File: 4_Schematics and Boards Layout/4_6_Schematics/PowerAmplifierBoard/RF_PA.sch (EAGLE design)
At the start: 25 parts, among them J1 142-0731-211, J2 142-0731-211, X2 22-23-2021, X3 22-23-2031

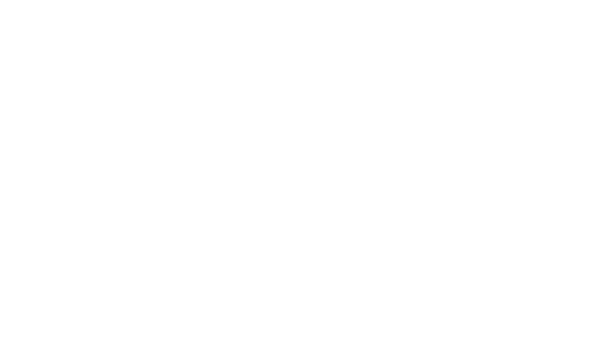
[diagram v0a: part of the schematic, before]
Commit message: feat(hw): gate-bias fail-safe, negative-rail margin, PA drain bulk (Lane B B2.2/B1.5/B2.3)
B2.2 -- and this is the finding that matters.  Every one of the 16 gate-bias
channels is an inverting amplifier referenced to ground (Vout = -(Rf/Rin) x VDAC,
+ input on GND), so a DAC in reset puts **0 V on all 16 gates**.  QPA2962 is a
depletion-mode GaN HEMT, where 0 V means *fully on* -- with 22 V on the drains.
That is a power-up hazard, not a nuance.

The plan frames the fix as hardware default *plus* MCU sequence; the hardware half
is here.  One 10k pull-down per channel from VGn to the same negative rail that
supplies its op-amp (R178-R193), so the gates sit at the negative rail whenever
the op-amps are not actively driving: during power-up, power-down, and if an
op-amp is unpowered.  Deliberately not attempted: forcing the gates negative while
the op-amp *is* driving, which would mean moving the + input off ground and
re-characterising all 16 bias channels -- a topology decision with firmware
consequences, recorded rather than guessed.

B1.5 -- the same move feeds it: the four OPA4703 V- pins leave -5V5_PA, whose
LM2662 is at 100 % of rating, for -5V0_ADAR12/34 at ~60 % (two op-amps per rail).
Channels pull down to the rail their own op-amp runs from, so the LM2662 is off
the gate-bias path entirely.

B2.3 -- PA drain bulk was ~20 uF against the ~100 uF the 30 us / 1.68 A pulse
wants; eight more 10 uF 1206 ceramics (C10-C17) on VIN_M use the device this board
already carries, so no new footprint.

Verified: all four files parse (main 2009 parts / 822 elements, PA 51 / 33); no
OPA V- pin or pad remains on -5V5_PA and each ADAR rail carries two op-amps and
eight pull-downs; every VGn net gained exactly one new pull-down (its existing
feedback resistor is the other R on the net); the eight new caps are on VIN_M and
GND; no duplicate designators; gates green.  Both BOMs keep the repo's grouping --
the 10k/R0201 and 10uF/C1206 rows were extended rather than duplicated.

Un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
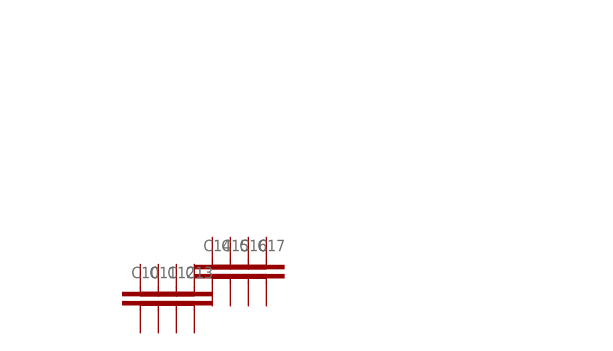
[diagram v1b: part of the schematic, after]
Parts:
- added C10, C11, C12, C13, C14, C15, C16, C17: 10µF, rcl:C-EUC1206
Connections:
- net GND: now also C10.2, C11.2, C12.2, C13.2, C14.2, C15.2, C16.2, C17.2
- net VIN_M: now also C10.1, C11.1, C12.1, C13.1, C14.1, C15.1, C16.1, C17.1
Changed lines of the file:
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@@
 <part name="GND18" library="supply1" library_urn="urn:adsk.eagle:library:371" deviceset="GND" device=""/>
 <part name="GND19" library="supply1" library_urn="urn:adsk.eagle:library:371" deviceset="GND" device=""/>
-<part name="U$1" library="My_Library_RADAR" deviceset="QPA2962_B" device=""/>
+<part name="C10" library="rcl" deviceset="C-EU" device="C1206" value="10µF"/><part name="C11" library="rcl" deviceset="C-EU" device="C1206" value="10µF"/><part name="C12" library="rcl" deviceset="C-EU" device="C1206" value="10µF"/><part name="C13" library="rcl" deviceset="C-EU" device="C1206" value="10µF"/><part name="C14" library="rcl" deviceset="C-EU" device="C1206" value="10µF"/><part name="C15" library="rcl" deviceset="C-EU" device="C1206" value="10µF"/><part name="C16" library="rcl" deviceset="C-EU" device="C1206" value="10µF"/><part name="C17" library="rcl" deviceset="C-EU" device="C1206" value="10µF"/><part name="U$1" library="My_Library_RADAR" deviceset="QPA2962_B" device=""/>
 <part name="FRAME1" library="frames" library_urn="urn:adsk.eagle:library:229" deviceset="A4-SMALL-DOCFIELD" device=""/>
 </parts>
@@
 <attribute name="VALUE" x="22.86" y="88.9" size="1.778" layer="96"/>
 </instance>
-<instance part="U$1" gate="G$1" x="91.44" y="100.33" smashed="yes"/>
+<instance part="C10" gate="G$1" x="22" y="34" smashed="yes"><attribute name="NAME" x="21" y="35" size="1.27" layer="95"/></instance><instance part="C11" gate="G$1" x="24" y="34" smashed="yes"><attribute name="NAME" x="23" y="35" size="1.27" layer="95"/></instance><instance part="C12" gate="G$1" x="26" y="34" smashed="yes"><attribute name="NAME" x="25" y="35" size="1.27" layer="95"/></instance><instance part="C13" gate="G$1" x="28" y="34" smashed="yes"><attribute name="NAME" x="27" y="35" size="1.27" layer="95"/></instance><instance part="C14" gate="G$1" x="30" y="37" smashed="yes"><attribute name="NAME" x="29" y="38" size="1.27" layer="95"/></instance><instance part="C15" gate="G$1" x="32" y="37" smashed="yes"><attribute name="NAME" x="31" y="38" size="1.27" layer="95"/></instance><instance part="C16" gate="G$1" x="34" y="37" smashed="yes"><attribute name="NAME" x="33" y="38" size="1.27" layer="95"/></instance><instance part="C17" gate="G$1" x="36" y="37" smashed="yes"><attribute name="NAME" x="35" y="38" size="1.27" layer="95"/></instance><instance part="U$1" gate="G$1" x="91.44" y="100.33" smashed="yes"/>
 <instance part="FRAME1" gate="/1" x="1.27" y="1.27" smashed="yes">
 <attribute name="LAST_DATE_TIME" x="102.87" y="7.62" size="2.54" layer="94"/>
@@
 <pinref part="GND15" gate="1" pin="GND"/>
 <wire x1="48.26" y1="184.15" x2="48.26" y2="182.88" width="0.1524" layer="91"/>
-</segment>
+<pinref part="C10" gate="G$1" pin="2"/><pinref part="C11" gate="G$1" pin="2"/><pinref part="C12" gate="G$1" pin="2"/><pinref part="C13" gate="G$1" pin="2"/><pinref part="C14" gate="G$1" pin="2"/><pinref part="C15" gate="G$1" pin="2"/><pinref part="C16" gate="G$1" pin="2"/><pinref part="C17" gate="G$1" pin="2"/></segment>
 </net>
 <net name="N$5" class="0">
@@
 <wire x1="111.76" y1="151.13" x2="111.76" y2="120.65" width="0.1524" layer="91"/>
 <wire x1="111.76" y1="120.65" x2="106.68" y2="120.65" width="0.1524" layer="91"/>
-</segment>
+<pinref part="C10" gate="G$1" pin="1"/><pinref part="C11" gate="G$1" pin="1"/><pinref part="C12" gate="G$1" pin="1"/><pinref part="C13" gate="G$1" pin="1"/><pinref part="C14" gate="G$1" pin="1"/><pinref part="C15" gate="G$1" pin="1"/><pinref part="C16" gate="G$1" pin="1"/><pinref part="C17" gate="G$1" pin="1"/></segment>
 </net>
 <net name="N$10" class="0">
